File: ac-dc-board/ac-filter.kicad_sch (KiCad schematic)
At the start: 12 parts

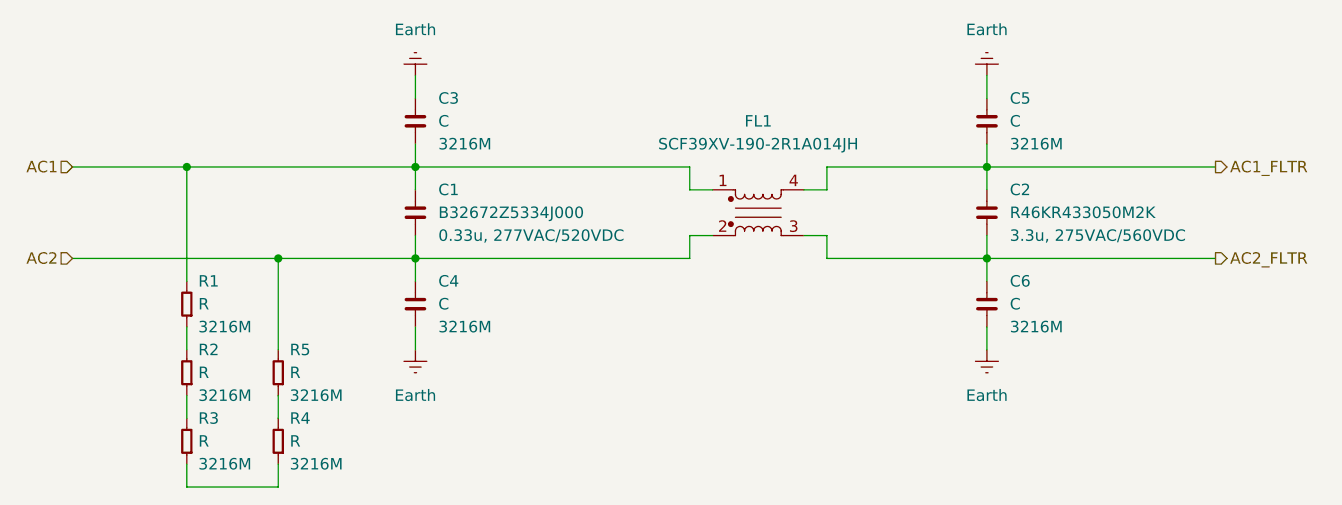
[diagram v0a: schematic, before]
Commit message: modify lavel name
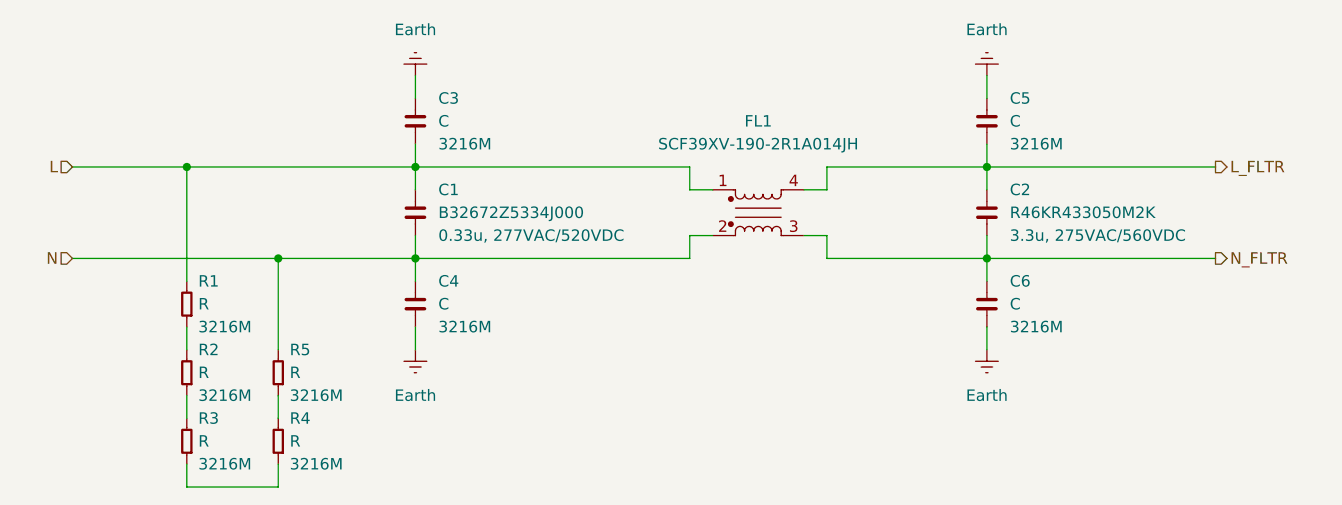
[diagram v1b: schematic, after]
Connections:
- net AC1 renamed L
- net AC1_FLTR renamed L_FLTR
- net AC2 renamed N
- net AC2_FLTR renamed N_FLTR
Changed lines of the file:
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@@
 		)
 	)
-	(hierarchical_label "AC1_FLTR"
+	(hierarchical_label "L_FLTR"
 		(shape output)
 		(at 165.1 45.72 0)
@@
 		)
 	)
-	(hierarchical_label "AC1"
+	(hierarchical_label "L"
 		(shape input)
 		(at 38.1 45.72 180)
@@
 		)
 	)
-	(hierarchical_label "AC2"
+	(hierarchical_label "N"
 		(shape input)
 		(at 38.1 55.88 180)
@@
 		)
 	)
-	(hierarchical_label "AC2_FLTR"
+	(hierarchical_label "N_FLTR"
 		(shape output)
 		(at 165.1 55.88 0)
